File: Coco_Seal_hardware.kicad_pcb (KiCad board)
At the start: 2 copper layers, 48.5 x 77 mm, 43 parts, among them J1 E220-900T22S(JP), Q1 FS8205A, Q3 Q_NMOS_GSD, SW1 SW_Push, SW2 SW_Push, SW3 SW_Push, U1 TPD2EUSB30A, U2 ESP32-C3-WROOM-02, U3 TP4056-42-ESOP8, U5 AP2112K-3.3, U6 DW01A, U7 SSD1306_OLED

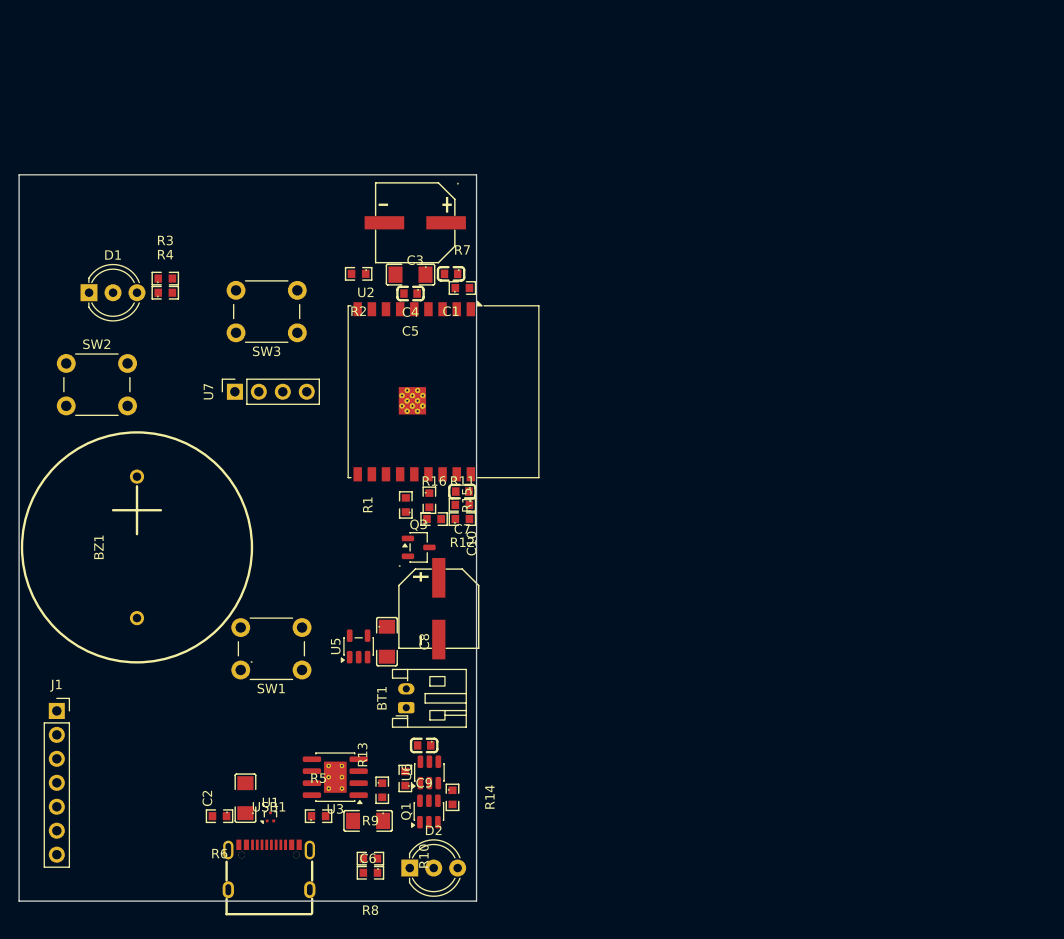
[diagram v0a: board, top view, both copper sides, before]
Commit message: 基板設計中3.3v配線途中
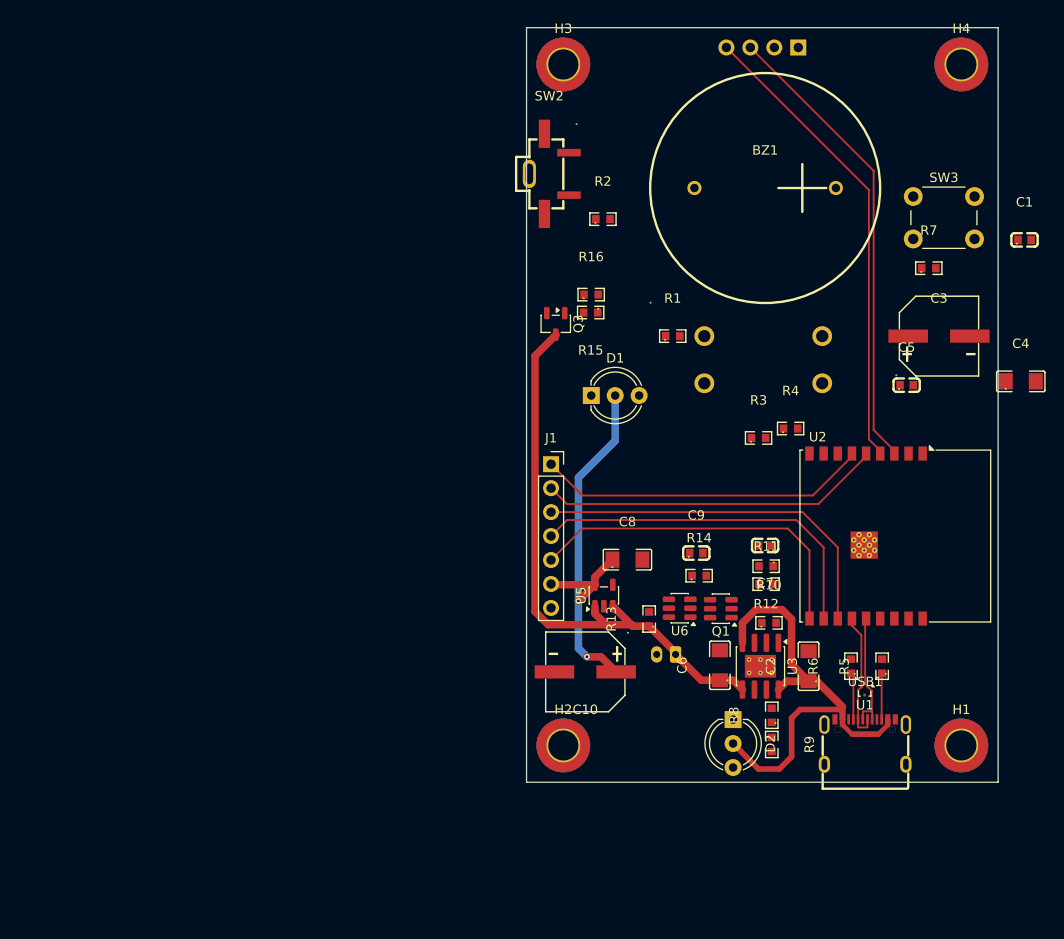
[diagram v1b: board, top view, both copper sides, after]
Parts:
- added H1: MountingHole_Pad, MountingHole:MountingHole_3.2mm_M3_ISO7380_Pad_TopBottom, F.Cu at (198.4, 139.5)
- added H2: MountingHole_Pad, MountingHole:MountingHole_3.2mm_M3_ISO7380_Pad_TopBottom, F.Cu at (156.2, 139.5)
- added H3: MountingHole_Pad, MountingHole:MountingHole_3.2mm_M3_ISO7380_Pad_TopBottom, F.Cu at (156.2, 67.3)
- added H4: MountingHole_Pad, MountingHole:MountingHole_3.2mm_M3_ISO7380_Pad_TopBottom, F.Cu at (198.4, 67.3)
- BT1, U7: moved to B.Cu
- SW1: value SW_Push -> SOS_Button; footprint Button_Switch_THT:SW_PUSH_6mm -> easyeda2kicad:SW-TH_4P-L12.0-W12.0-P5.00_TS-094; moved to B.Cu
- SW2: value SW_Push -> Common_Button; footprint Button_Switch_THT:SW_PUSH_6mm -> easyeda2kicad:SW-TH_TS665TPZJ
- SW3: value SW_Push -> Reset_Button
- moved BZ1 76.7 mm to (177.6, 80.4), turned to 0 degrees
- moved U7 70.0 mm to (181.1, 65.5)
- moved R6 68.8 mm to (186.7, 131.1), turned to 90 degrees
- moved R4 67.8 mm to (180.3, 105.9)
- moved SW3 66.9 mm to (193.3, 81.3), turned to 0 degrees
- moved C4 65.7 mm to (204.7, 100.9), turned to 0 degrees
- moved R3 65.1 mm to (176.9, 106.9)
- moved USB1 64.6 mm to (188.2, 139.1)
- moved U1 64.4 mm to (188.2, 133.7), turned to 180 degrees
- moved R5 61.8 mm to (190.0, 131.1), turned to 90 degrees
- moved C2 61.3 mm to (182.2, 131.1)
- moved C1 60.9 mm to (205.1, 85.9), turned to 0 degrees
- moved SW1 58.9 mm to (177.4, 98.6)
- moved J1 58.6 mm to (154.9, 109.7)
- moved C3 56.8 mm to (196.0, 96.1), turned to 0 degrees
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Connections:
- U7 pad 3: GPIO5 -> GPIO4
- U7 pad 4: GPIO4 -> GPIO5
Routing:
- net BATT+: track 0.00 -> 61.2 mm
- net 5V: track 0.00 -> 50.8 mm
- net GPIO5: track 0.00 -> 49.8 mm
- net GPIO4: track 0.00 -> 49.4 mm
- net 3.3V: track 0.00 -> 44.0 mm, vias 0 -> 2
- net UART_TXD: track 0.00 -> 39.5 mm
- net UART_RXD: track 0.00 -> 38.4 mm
- net GPIO10: track 0.00 -> 37.0 mm
- net GPIO6: track 0.00 -> 36.5 mm
- net GPIO7: track 0.00 -> 35.3 mm
- net GPIO18: track 0.00 -> 13.9 mm
- net GPIO19: track 0.00 -> 12.8 mm
- net Net-(USB1-CC1): track 0.00 -> 4.99 mm
- net Net-(USB1-CC2): track 0.00 -> 4.91 mm
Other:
- board size 48.5 x 77 mm -> 50 x 80 mm

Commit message: 配線いったん完了
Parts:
- SW1: footprint easyeda2kicad:SW-TH_4P-L12.0-W12.0-P5.00_TS-094 -> Button_Switch_THT:SW_PUSH-12mm
- moved R3 17.7 mm to (159.2, 107.6), turned to -90 degrees
- moved R4 16.2 mm to (164.2, 107.4), turned to -90 degrees
- moved C4 12.8 mm to (192.2, 103.7), turned to 180 degrees
- moved C9 8.36 mm to (165.3, 125.8), turned to -90 degrees
- moved SW1 6.51 mm to (183.8, 97.4)
- moved C1 6.30 mm to (199.8, 89.3), turned to -90 degrees
- moved C5 5.18 mm to (193.5, 106.4), turned to 180 degrees
- moved R1 3.61 mm to (167.5, 99.7)
- moved R10 2.42 mm to (177.7, 124.1)
- moved C8 2.27 mm to (164.5, 118.1)
- moved R14 2.06 mm to (172.6, 122.0)
- moved C3 2.05 mm to (195.6, 98.1)
- moved R13 1.81 mm to (163.5, 125.9)
- moved R2 1.65 mm to (162.0, 83.3), turned to 90 degrees
- moved R12 1.30 mm to (177.6, 119.2)
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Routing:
- net 3.3V: track 44.0 -> 158.8 mm, vias 2 -> 4
- net GPIO3: track 0.00 -> 46.3 mm, vias 0 -> 2
- net GPIO1: track 0.00 -> 44.1 mm, vias 0 -> 1
- net GPIO9: track 0.00 -> 39.9 mm
- net GPIO2: track 0.00 -> 38.1 mm, vias 0 -> 2
- net Net-(U2-EN): track 0.00 -> 36.0 mm
- net GPIO8: track 0.00 -> 29.3 mm
- net BATT+: track 61.2 -> 86.2 mm
- net GPIO0: track 0.00 -> 22.8 mm, vias 0 -> 2
- net Net-(BZ1-+): track 0.00 -> 22.7 mm, vias 0 -> 1
- net Net-(BT1--): track 0.00 -> 14.5 mm
- net Net-(U6-CS): track 0.00 -> 5.94 mm
- net Net-(U3-PROG): track 0.00 -> 5.84 mm, vias 0 -> 2
- net Net-(U3-~{STDBY}): track 0.00 -> 5.84 mm
- net Net-(D2-K2): track 0.00 -> 5.42 mm, vias 0 -> 1
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- added copper zone on B.Cu, net GND
- added copper zone on F.Cu, net GND

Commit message: JLCPCB用にデータを追加
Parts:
- moved R14 3.00 mm to (169.6, 122.0)
- moved SW2 0.45 mm to (155.6, 78.4)
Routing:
- net Net-(U6-CS): track 5.94 -> 3.61 mm
- net GND: vias 199 -> 203
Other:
- board text added: "Coco Seal Board v1.0"

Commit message: 基板設計いったん完了
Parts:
- D1: moved to B.Cu
- R8, R9: value 1k -> 1K
- moved R3 39.5 mm to (166.1, 68.7), turned to 0 degrees
- moved D1 33.8 mm to (161.2, 68.7), turned to -90 degrees
- moved R4 31.4 mm to (162.0, 76.1), turned to 0 degrees
- moved D2 4.98 mm to (174.1, 141.7), turned to 90 degrees
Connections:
- R8 pad 1: Net-(D2-K1) -> Net-(D2-K2)
- R9 pad 2: Net-(D2-K2) -> Net-(D2-K1)
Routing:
- net 3.3V: track 158.8 -> 192.6 mm, vias 4 -> 5
- net GPIO2: track 38.1 -> 67.7 mm
- net GPIO8: track 29.3 -> 49.7 mm
- net /Red: track 4.27 -> 2.38 mm
- net Net-(D2-K2): track 5.42 -> 4.35 mm
- net Net-(D2-K1): track 4.35 -> 5.42 mm
- net GND: vias 203 -> 211
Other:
- board text added: "+"
- board text added: "G"
- board text added: "GND"
- board text added: "R"
